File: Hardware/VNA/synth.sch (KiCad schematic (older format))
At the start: 35 parts, among them U3 MAX2871, X1 ASTXR-12-19.200MHz

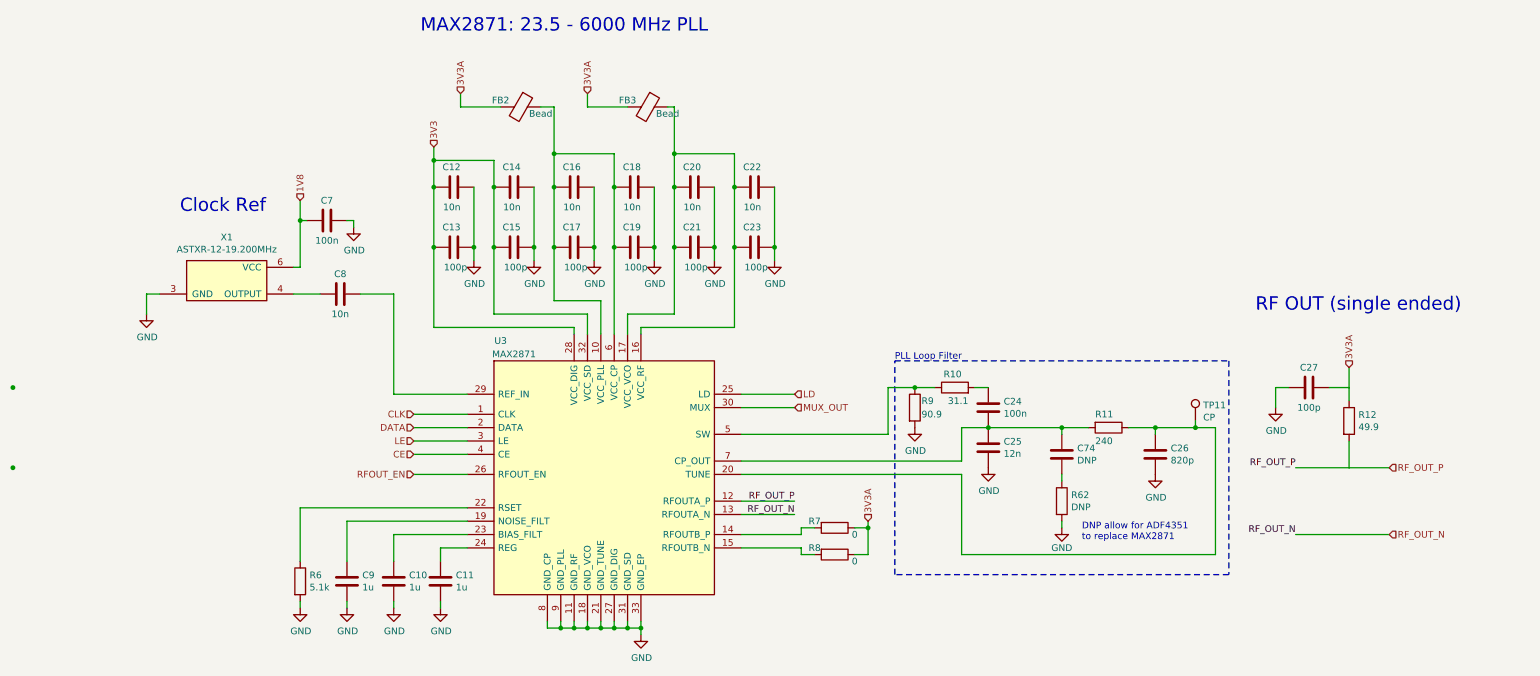
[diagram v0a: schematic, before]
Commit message: output level test code + schematic change to fix MAX output levels
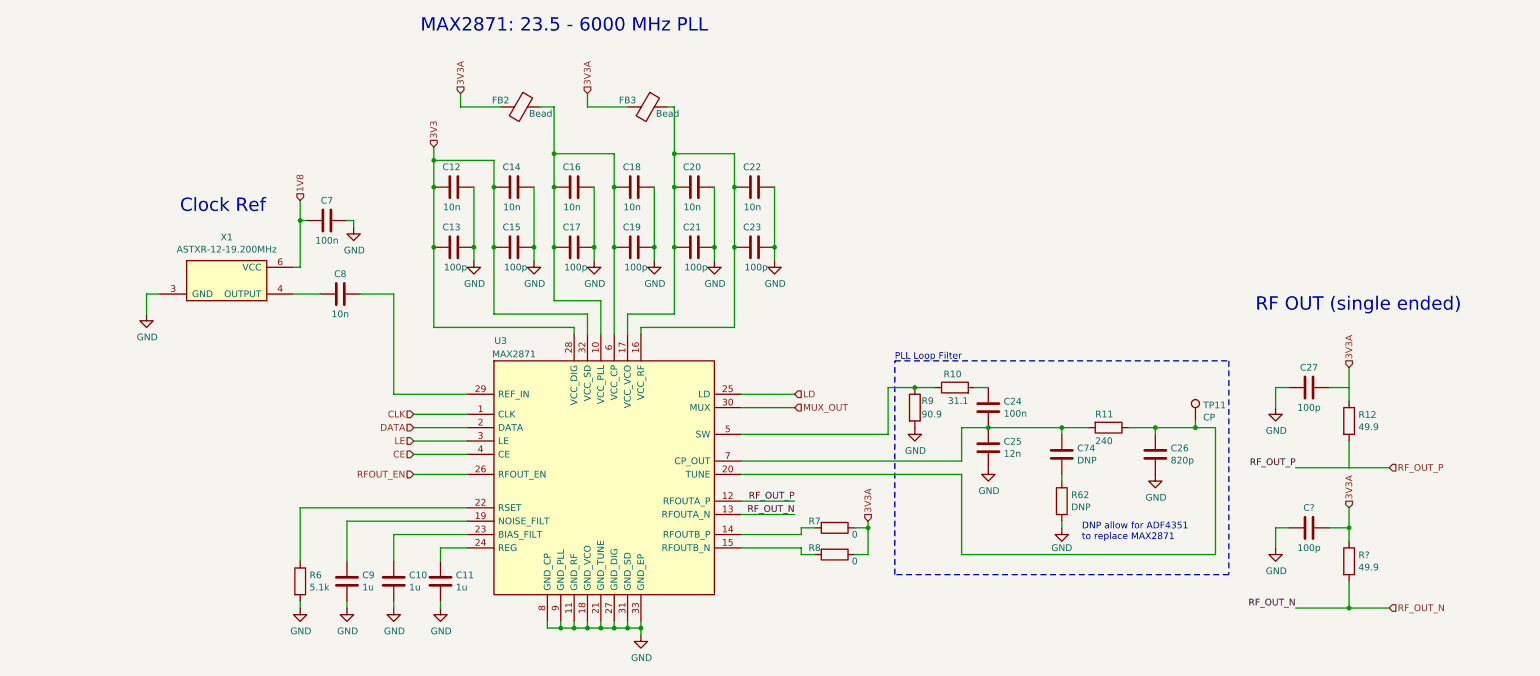
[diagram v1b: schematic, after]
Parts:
- added C?: 100p, Capacitor_SMD:C_0402_1005Metric, symbol Device:C
- added R?: 49.9, Resistor_SMD:R_0402_1005Metric, symbol Device:R
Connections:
- net 3V3A: now also C?.1, R?.1
- net GND: now also C?.2
- net RF_OUT_N: now also R?.2
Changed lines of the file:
@@
 	4950 1900 4950 2250
 Connection ~ 4950 2250
-Text Label 9600 5100 2    50   ~ 0
+Text Label 9600 5650 2    50   ~ 0
 RF_OUT_N
 Text Label 9600 4600 2    50   ~ 0
@@
 	1    0    0    -1
 $EndComp
-Connection ~ 0    4000
 Wire Wire Line
 	10000 4000 10000 4100
@@
 $EndComp
 Wire Wire Line
-	9600 5100 10300 5100
+	9600 5650 10000 5650
 Wire Wire Line
 	10000 4400 10000 4600
-Connection ~ 0    4600
 Wire Wire Line
 	10000 4600 10300 4600
@@
 Text HLabel 10300 4600 2    50   Input ~ 0
 RF_OUT_P
-Text HLabel 10300 5100 2    50   Input ~ 0
+Text HLabel 10300 5650 2    50   Input ~ 0
 RF_OUT_N
 Text HLabel 5850 4050 2    50   Input ~ 0
@@
 Wire Wire Line
 	8850 4300 9000 4300
+$Comp
+L Device:R R?
+U 1 1 5D23DFFB
+P 10000 5300
+F 0 "R?" H 10070 5346 50  0000 L CNN
+F 1 "49.9" H 10070 5255 50  0000 L CNN
+F 2 "Resistor_SMD:R_0402_1005Metric" V 9930 5300 50  0001 C CNN
+F 3 "~" H 10000 5300 50  0001 C CNN
+	1    10000 5300
+	1    0    0    -1
+$EndComp
+$Comp
+L Device:C C?
+U 1 1 5D23E001
+P 9700 5050
+F 0 "C?" V 9550 5050 50  0000 C CNN
+F 1 "100p" V 9850 5050 50  0000 C CNN
+F 2 "Capacitor_SMD:C_0402_1005Metric" H 9738 4900 50  0001 C CNN
+F 3 "~" H 9700 5050 50  0001 C CNN
+	1    9700 5050
+	0    1    1    0
+$EndComp
+Wire Wire Line
+	9850 5050 10000 5050
+Wire Wire Line
+	9550 5050 9450 5050
+Wire Wire Line
+	9450 5050 9450 5200
+$Comp
+L power:GND #PWR?
+U 1 1 5D23E00A
+P 9450 5200
+F 0 "#PWR?" H 9450 4950 50  0001 C CNN
+F 1 "GND" H 9455 5027 50  0000 C CNN
+F 2 "" H 9450 5200 50  0001 C CNN
+F 3 "" H 9450 5200 50  0001 C CNN
+	1    9450 5200
+	1    0    0    -1
+$EndComp
+Wire Wire Line
+	10000 5050 10000 5150
+Wire Wire Line
+	10000 4900 10000 5050
+Wire Wire Line
+	10000 5450 10000 5650
+Text HLabel 10000 4900 1    50   Input ~ 0
+3V3A
+Connection ~ 10000 5650
+Wire Wire Line
+	10000 5650 10300 5650
+Connection ~ 10000 5050
 $EndSCHEMATC
